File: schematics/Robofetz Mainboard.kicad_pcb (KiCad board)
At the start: 2 copper layers, 11 parts, among them J1 On/Off Switch, J2 Battery Connector, J3 Conn_01x04_Pin, J4 Motor 1, J5 Motor 2, J6 Weapon Controller, U2 DCDC, U3 ROB-14450, U4 ESP32, U5 ESP32-DevKitC

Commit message: Finished PCB Version 1
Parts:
- moved D1 61.1 mm to (95.4, 103.4), turned to 180 degrees
- moved J5 56.2 mm to (156.4, 105.1), turned to -90 degrees
- moved U5 47.6 mm to (110.1, 83.3)
- moved J4 42.8 mm to (143.2, 105.0), turned to -90 degrees
- moved U3 38.6 mm to (150.0, 75.6)
- moved U4 30.5 mm to (104.4, 83.1)
- moved J1 17.3 mm to (89.5, 86.0)
- moved J2 17.3 mm to (81.5, 86.2)
- moved J3 17.3 mm to (81.2, 103.0)
- moved J6 17.3 mm to (96.5, 90.2)
- moved U2 17.3 mm to (97.3, 119.5)
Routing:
- net GND: track 0.00 -> 269.8 mm
- net Supply 3.3V: track 0.00 -> 131.3 mm
- net Motor 2 PWM: track 0.00 -> 95.9 mm
- net Motor2 CCW: track 0.00 -> 88.7 mm
- net Encoder L2: track 0.00 -> 84.8 mm
- net Supply 16V: track 0.00 -> 84.3 mm
- net Motor2 CW: track 0.00 -> 81.7 mm
- net Encoder L1: track 0.00 -> 77.3 mm
- net STBY: track 0.00 -> 63.8 mm
- net WPN Control: track 0.00 -> 56.6 mm
- net Motor1 CW: track 0.00 -> 56.5 mm
- net Motor 1 PWM: track 0.00 -> 40.7 mm
- net Motor1 CCW: track 0.00 -> 40.6 mm
- net Motor 1 - 2: track 0.00 -> 38.1 mm
- net Encoder R2: track 0.00 -> 31.4 mm
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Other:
- board outline added: 86 x 61 mm
- board text added: "+"

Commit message: updated schematics + pcb layout
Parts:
- added R1: R, Resistor_THT:R_Axial_DIN0204_L3.6mm_D1.6mm_P1.90mm_Vertical, F.Cu at (100.4, 88.0)
- added R2: R, Resistor_THT:R_Axial_DIN0204_L3.6mm_D1.6mm_P1.90mm_Vertical, F.Cu at (100.4, 84.0)
- moved J6 13.4 mm to (98.5, 103.5)
- moved D1 13.3 mm to (98.5, 116.3), turned to 90 degrees
- moved J3 12.3 mm to (92.5, 108.0), turned to -90 degrees
- moved U2 11.8 mm to (109.0, 117.8), turned to 0 degrees
- moved J2 11.6 mm to (93.0, 84.5)
- moved J1 11.5 mm to (91.8, 97.2)
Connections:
- J1 pad 1: Supply 16V -> Net-(J1-Pin_1)
- J1 pad 2: Net-(J1-Pin_2) -> Supply 16V
- J2 pad 1: Supply 16V -> Net-(J1-Pin_1)
- J2 pad 2: Net-(J2-Pin_2) -> GND
- J3 pad 1: Net-(J3-Pin_1) -> GND
- J3 pad 3: Net-(J1-Pin_2) -> Supply 16V
- J3 pad 4: Net-(J2-Pin_2) -> GND
- J6 pad 2: WPN Control -> Net-(J6-Pin_2)
- J6 pad 3: Supply 16V -> Supply 3.3V
- U2 pad 2: Net-(J3-Pin_1) -> GND
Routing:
- net Supply 3.3V: track 131.3 -> 158.5 mm
- net GND: track 269.8 -> 291.4 mm
- net Net-(J6-Pin_2): track 0.00 -> 18.1 mm
- net Supply 16V: track 84.3 -> 102.2 mm
- net Net-(J1-Pin_1): track 0.00 -> 13.5 mm
- net Net-(J1-Pin_2): track 12.9 -> 0.00 mm
- net Net-(J3-Pin_1): track 6.87 -> 0.00 mm
- net Net-(J2-Pin_2): track 6.85 -> 0.00 mm
- net Motor1 CCW: track 40.6 -> 34.5 mm, vias 0 -> 1
- net Motor 1 PWM: track 40.7 -> 36.9 mm, vias 0 -> 1
- net Supply 5V: track 19.0 -> 15.3 mm
- net WPN Control: track 56.6 -> 53.7 mm, vias 0 -> 2
- net Net-(D1-A): track 7.74 -> 6.75 mm
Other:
- board size 86 x 61 mm -> 76.5 x 61 mm
- board text added: "-"
- board text added: "Battery"
- board text added: "DCDC"
- board text added: "Motor 1"
- board text added: "Motor 2"
- board text added: "Motor Controller"
- board text added: "On/Off switch"
- board text added: "Remote Killswitch"
- board text added: "Weapon Controller"

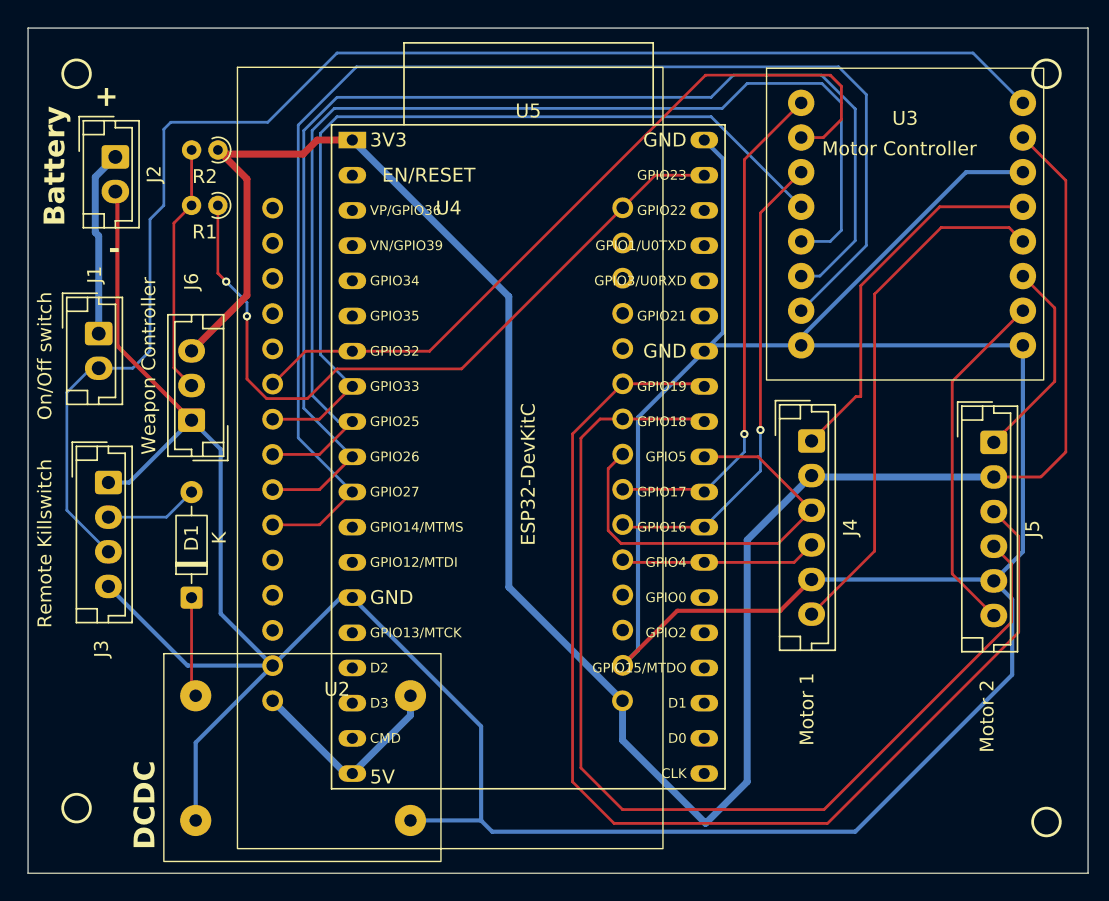
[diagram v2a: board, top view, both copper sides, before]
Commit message: updated layout
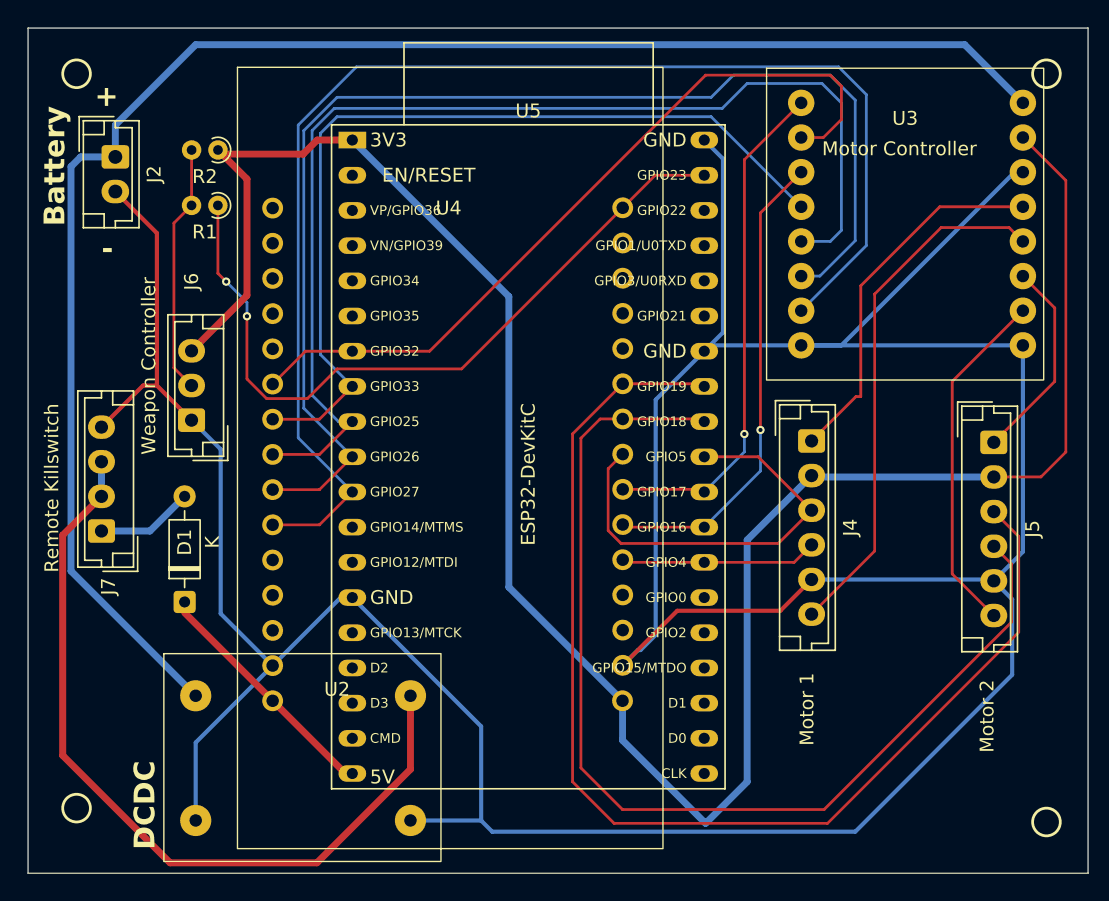
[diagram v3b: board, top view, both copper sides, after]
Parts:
- removed J1: On/Off Switch, Connector_JST:JST_EH_B2B-EH-A_1x02_P2.50mm_Vertical
- removed J3: Conn_01x04_Pin, Connector_JST:JST_EH_B4B-EH-A_1x04_P2.50mm_Vertical
- added J7: Conn_01x04_Pin, Connector_JST:JST_EH_B4B-EH-A_1x04_P2.50mm_Vertical, F.Cu at (92.0, 111.5)
- J2: value Battery Connector -> PCB Power Connector
- moved D1 0.59 mm to (98.0, 116.6)
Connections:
- D1 pad 1: Net-(D1-K) -> Supply 5V ESP
- J2 pad 1: Net-(J1-Pin_1) -> Supply 16V
- U2 pad 1: Net-(D1-K) -> Supply 16V
- U4 pad 0: Supply 5V -> Supply 5V ESP
- U5 pad 19: Supply 5V -> Supply 5V ESP
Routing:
- net Supply 5V: track 15.3 -> 60.2 mm
- net Supply 5V ESP: track 0.00 -> 18.2 mm
- net GND: track 291.4 -> 274.3 mm
- net Supply 16V: track 102.2 -> 117.8 mm
- net Net-(J1-Pin_1): track 13.5 -> 0.00 mm
- net Net-(D1-K): track 7.20 -> 0.00 mm
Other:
- board text removed: "On/Off switch"

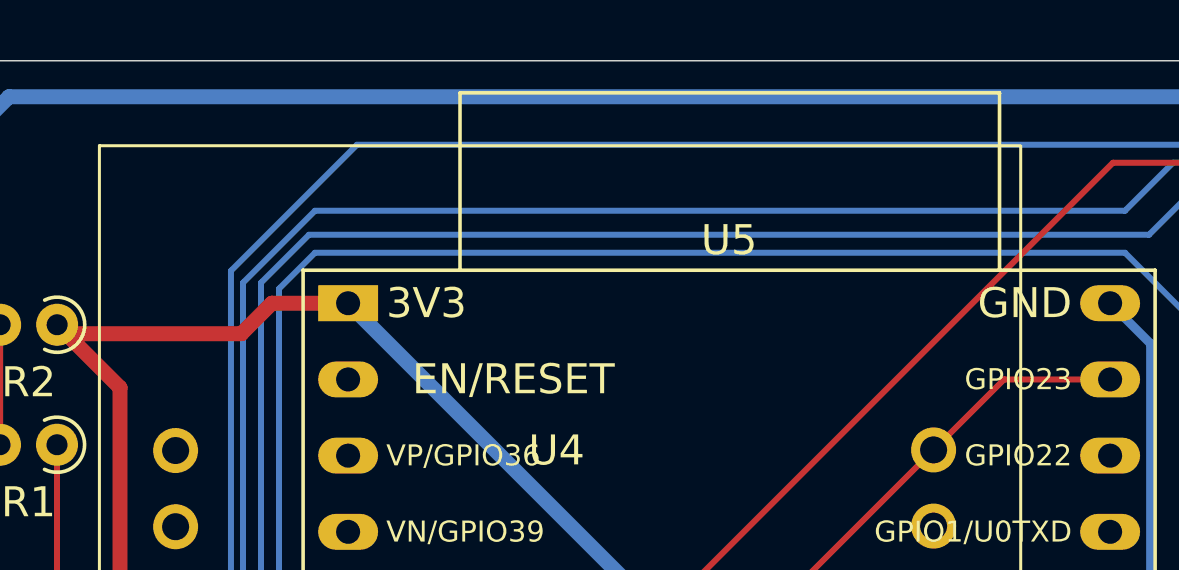
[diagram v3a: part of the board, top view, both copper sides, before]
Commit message: Updated layout
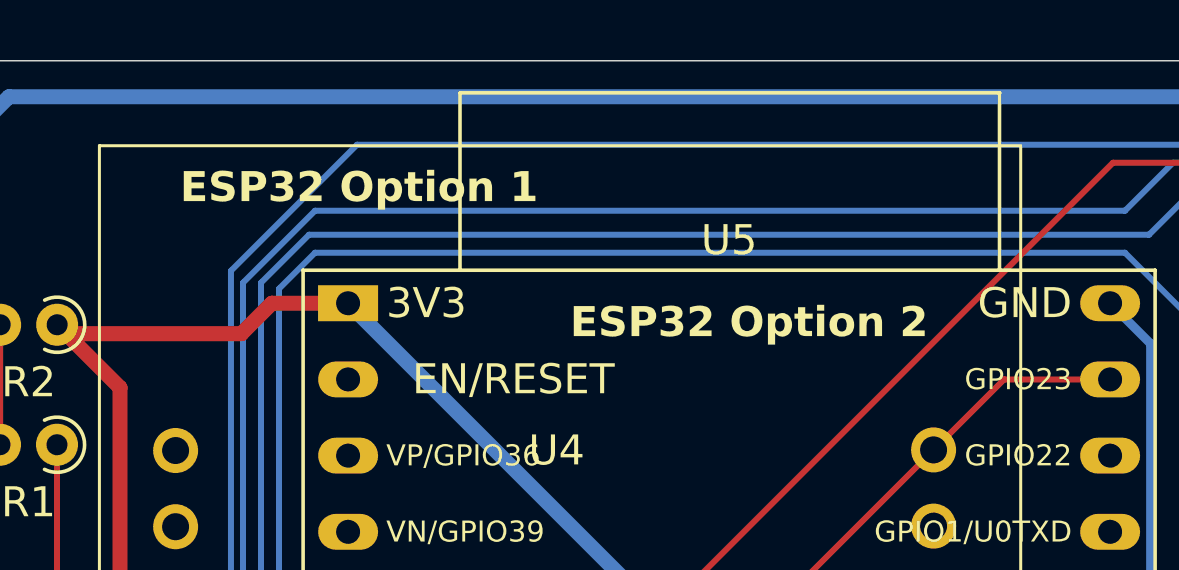
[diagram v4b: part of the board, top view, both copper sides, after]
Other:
- board text added: "ESP32 Option 1"
- board text added: "ESP32 Option 2"
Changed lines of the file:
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@@
+		)
+	)
+	(gr_text "ESP32 Option 1"
+		(at 104.5 80 0)
+		(layer "F.SilkS")
+		(effects
+			(font
+				(size 1 1)
+				(thickness 0.2)
+				(bold yes)
+			)
+			(justify left bottom)
+		)
+	)
+	(gr_text "ESP32 Option 2"
+		(at 117.5 84.5 0)
+		(layer "F.SilkS")
+		(effects
+			(font
+				(size 1 1)
+				(thickness 0.2)
+				(bold yes)
+			)
+			(justify left bottom)
 		)
 	)

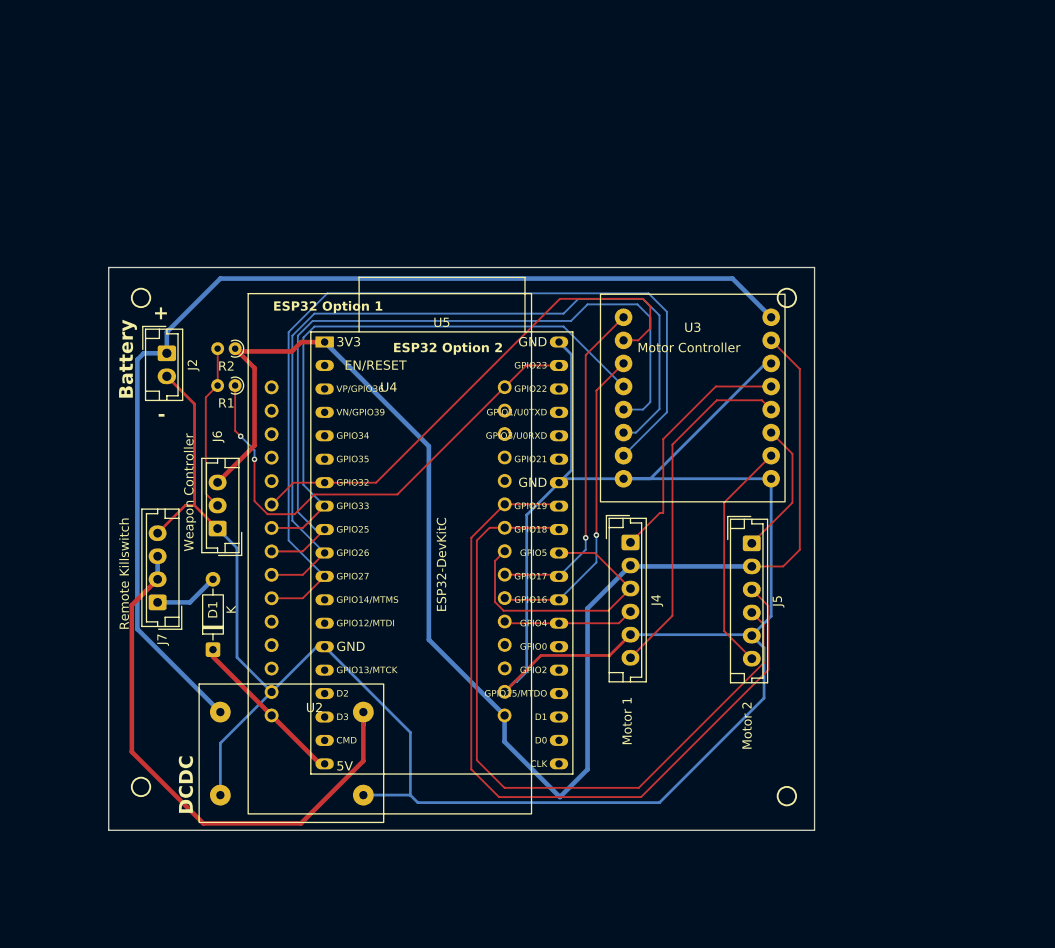
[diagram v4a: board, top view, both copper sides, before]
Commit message: updated layout
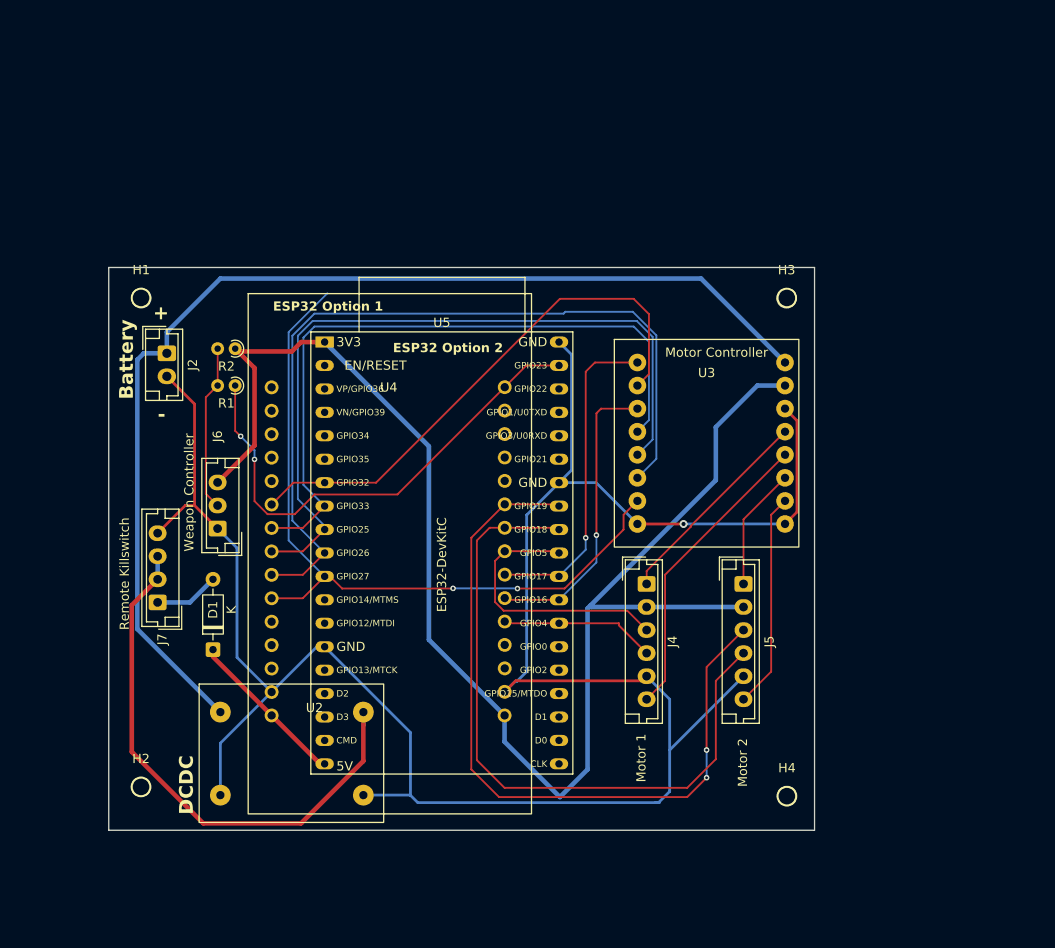
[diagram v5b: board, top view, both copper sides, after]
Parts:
- added H1: MountingHole, MountingHole:MountingHole_2.1mm, F.Cu at (90.2, 78.5)
- added H2: MountingHole, MountingHole:MountingHole_2.1mm, F.Cu at (90.2, 131.5)
- added H3: MountingHole, MountingHole:MountingHole_2.1mm, F.Cu at (160.2, 78.5)
- added H4: MountingHole, MountingHole:MountingHole_2.1mm, F.Cu at (160.2, 132.5)
- moved U3 5.12 mm to (151.5, 80.5)
- moved J4 4.83 mm to (145.0, 109.5)
- moved J5 4.49 mm to (155.5, 109.5)
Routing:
- net GND: track 274.3 -> 242.8 mm, vias 0 -> 1
- net Motor 2 PWM: track 95.9 -> 80.1 mm, vias 0 -> 2
- net STBY: track 63.8 -> 74.8 mm
- net Motor 1 - 2: track 38.1 -> 32.7 mm
- net Motor 1 - 1: track 26.9 -> 22.7 mm
- net Supply 16V: track 117.8 -> 121.3 mm
- net Encoder L2: track 84.8 -> 81.5 mm, vias 0 -> 2
- net Encoder L1: track 77.3 -> 74.5 mm
- net Encoder R1: track 14.2 -> 16.9 mm
- net Motor1 CW: track 56.5 -> 59.1 mm
- net Motor 2 - 1: track 25.4 -> 23.4 mm
- net Motor1 CCW: track 34.5 -> 32.5 mm
- net Encoder R2: track 31.4 -> 29.6 mm
- net Supply 3.3V: track 158.5 -> 160.3 mm
- net Motor 1 PWM: track 36.9 -> 35.4 mm
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
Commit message: updated lazout
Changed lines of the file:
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@@
 			(outputformat 1)
 			(mirror no)
-			(drillshape 1)
+			(drillshape 0)
 			(scaleselection 1)
 			(outputdirectory "")
@@
 		(tags "mountinghole")
 		(property "Reference" "H3"
-			(at 0 -3.05 0)
+			(at 0 3.471743 0)
 			(layer "F.SilkS")
 			(effects
@@
 		(tags "mountinghole")
 		(property "Reference" "H1"
-			(at 0 -3.05 0)
+			(at 3.783279 -0.51806 0)
 			(layer "F.SilkS")
 			(effects
@@
 		(tags "mountinghole")
 		(property "Reference" "H2"
-			(at 0 -3.05 0)
+			(at -0.198661 3.5 0)
 			(layer "F.SilkS")
 			(effects
@@
 		(tags "mountinghole")
 		(property "Reference" "H4"
-			(at 0 -3.05 0)
+			(at 0.292309 -3.499999 0)
 			(layer "F.SilkS")
 			(effects
